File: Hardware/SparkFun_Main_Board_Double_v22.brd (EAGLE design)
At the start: 124.5 x 73.7 mm, 134 parts, among them J1 MICROMOD-2222-C, J10 MICRO-SD-PUSH-PUSH-EXT-PIN, J2 Vertical Qwiic Connector, J4 QWIIC_RIGHT_ANGLE, J5 CORTEX_JTAG_DEBUG_MINIMUM_PTH, J6 MICROMOD_FUNCTION_MAIN, J7 MICROMOD_FUNCTION_MAIN, Q1 3.1A/30V/105mΩ, Q2 20V/4.2A/52mΩ/1.4W, U1 STG3856QTR, U2 MCP73831, U3 ESD Diode, U4 AP7347DQ-33W5-7K-3.3V, U5 AP7361C-33

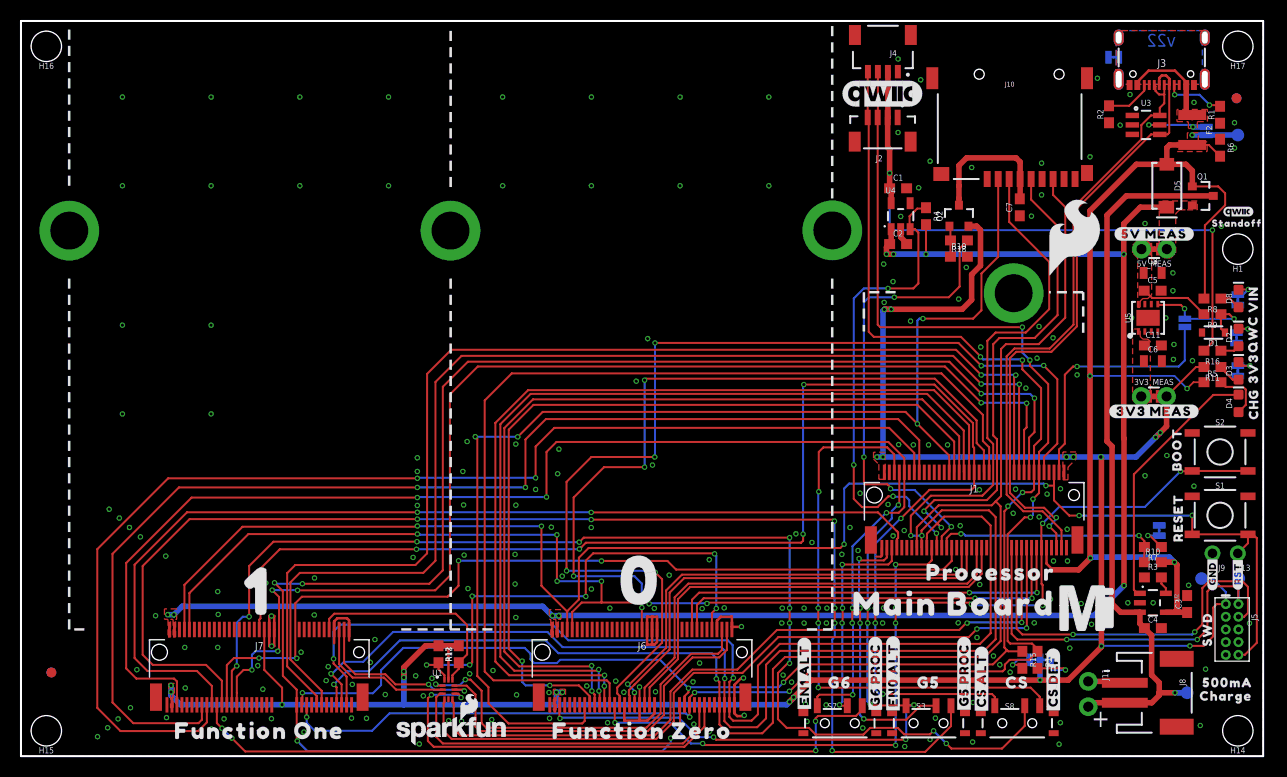
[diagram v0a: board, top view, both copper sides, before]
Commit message: Rotates 2 pin JST connector
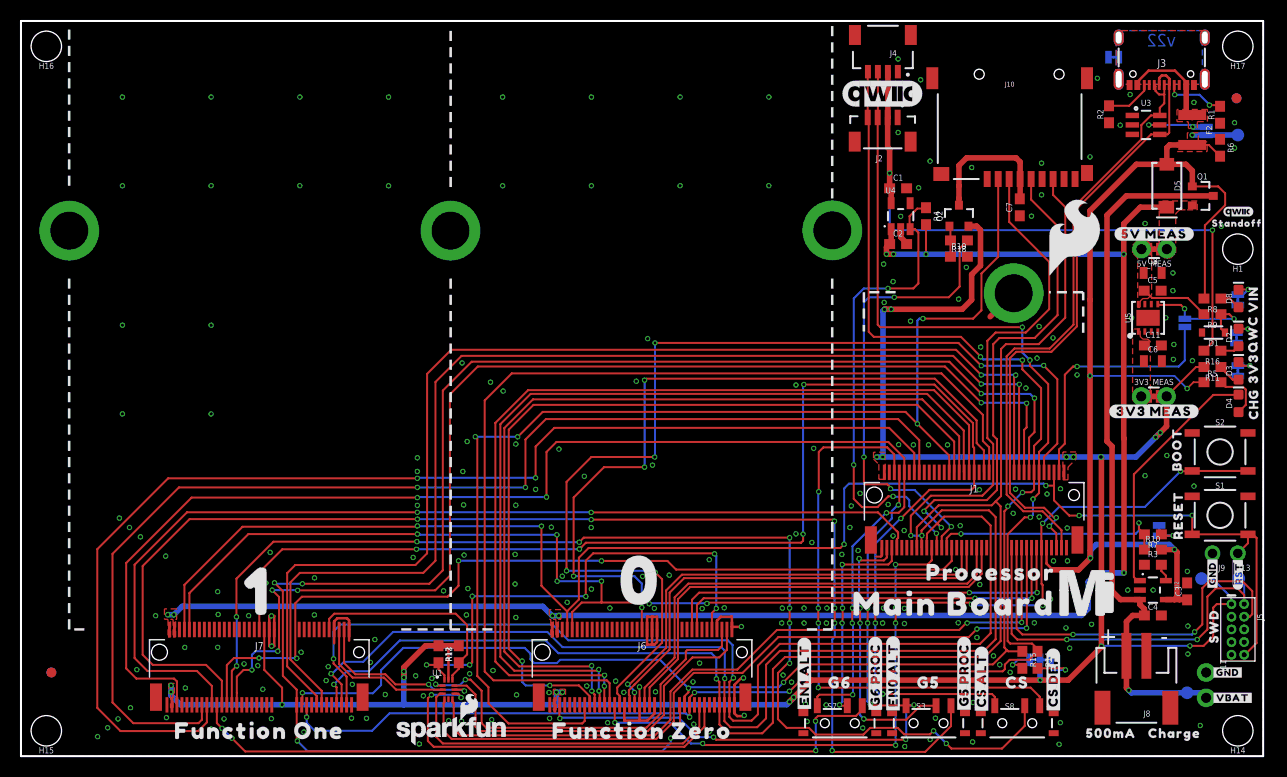
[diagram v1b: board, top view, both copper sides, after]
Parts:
- added U$3: (no value), top:##RST##8
- added U$46: (no value), top:#VBAT#9
- U$39: device top:#RST#6521 -> top:#GND#10
- U$40: device top:#GND#6520 -> top:#GND#10
- moved U$33 12.7 mm to (109.2, 2.29)
- moved J11 11.8 mm to (118.7, 8.38)
- moved U$40 10.0 mm to (120.9, 8.38), turned to 0 degrees
- moved U$27 6.37 mm to (115.6, 2.29)
- moved U$39 2.54 mm to (119.4, 18.3)
- moved J8 2.54 mm to (111.8, 6.35), turned to 180 degrees
- moved U$14 1.52 mm to (106.8, 16.4)
- moved R7 1.27 mm to (113.4, 22.2)
- moved C3 1.27 mm to (116.8, 16.5)
- moved C4 1.27 mm to (113.4, 14.1)
- moved R10 1.27 mm to (113.4, 20.7)
- moved R3 1.27 mm to (113.4, 19.2)
- moved U2 1.27 mm to (113.4, 16.6)
- moved U$25 0.73 mm to (119.5, 13.0)
- moved J5 0.57 mm to (121.9, 12.7)
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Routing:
- net V_BATT: track 73.2 -> 71.3 mm
- net N$14: track 26.1 -> 24.8 mm
- net VCC: track 168.5 -> 169.3 mm
- net VIN/3: track 23.4 -> 24.2 mm
- net 3.3V: track 236.2 -> 237.0 mm
- net VIN: track 112.8 -> 113.6 mm
- net !RESET!: track 155.0 -> 154.4 mm
- net GND: track 49.9 -> 49.6 mm, vias 219 -> 233

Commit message: Pushes JST 0.1" further into the board
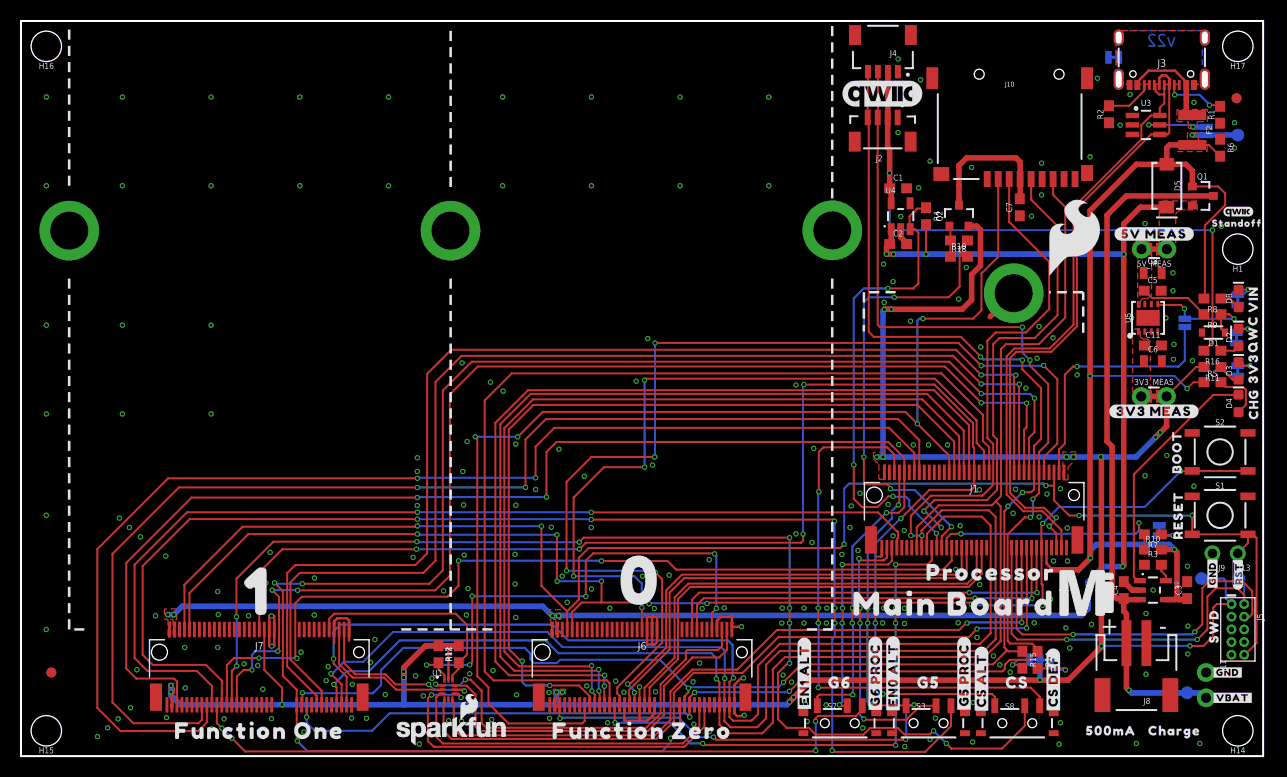
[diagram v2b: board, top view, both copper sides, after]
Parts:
- moved C4 3.87 mm to (110.5, 16.6), turned to 90 degrees
- moved J8 1.27 mm to (111.8, 7.62)
- moved U$8 0.25 mm to (115.8, 30.5)
- moved U$27 0.25 mm to (115.6, 2.54)
- moved U$33 0.25 mm to (109.2, 2.54)
- moved C3 0.13 mm to (116.8, 16.6)
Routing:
- net GND: track 49.6 -> 51.6 mm, vias 233 -> 241
- net V_BATT: track 71.3 -> 70.1 mm
- net 3.3V: track 237.0 -> 237.7 mm

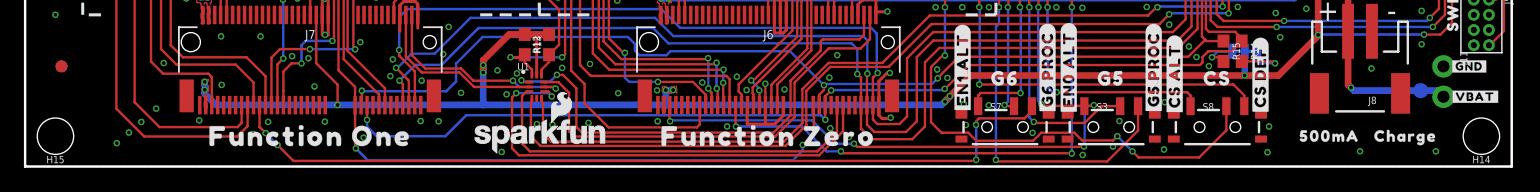
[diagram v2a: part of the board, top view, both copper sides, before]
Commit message: Adds notch for lipo battery, moves VBAT test point
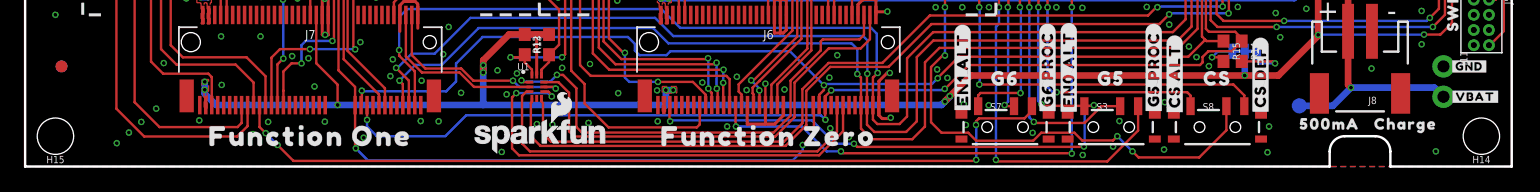
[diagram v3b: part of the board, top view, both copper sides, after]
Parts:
- moved TP3 10.2 mm to (106.7, 5.08)
- moved U$27 1.02 mm to (115.6, 3.56)
- moved U$33 1.02 mm to (109.2, 3.56)
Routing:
- net V_BATT: track 70.1 -> 75.0 mm
- net GND: vias 241 -> 240
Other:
- outline, holes or cut-outs redrawn
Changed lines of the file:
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@@
 <layer number="37" name="tTest" color="7" fill="1" visible="no" active="yes"/>
 <layer number="38" name="bTest" color="7" fill="1" visible="no" active="yes"/>
-<layer number="39" name="tKeepout" color="4" fill="11" visible="yes" active="yes"/>
+<layer number="39" name="tKeepout" color="4" fill="11" visible="no" active="yes"/>
 <layer number="40" name="bKeepout" color="1" fill="11" visible="no" active="yes"/>
 <layer number="41" name="tRestrict" color="4" fill="10" visible="no" active="yes"/>
@@
 <layer number="45" name="Holes" color="7" fill="1" visible="yes" active="yes"/>
 <layer number="46" name="Milling" color="3" fill="1" visible="no" active="yes"/>
-<layer number="47" name="Measures" color="7" fill="1" visible="no" active="yes"/>
+<layer number="47" name="Measures" color="7" fill="1" visible="yes" active="yes"/>
 <layer number="48" name="Document" color="7" fill="1" visible="no" active="yes"/>
 <layer number="49" name="Reference" color="13" fill="1" visible="yes" active="yes"/>
@@
 <plain>
 <wire x1="0" y1="73.66" x2="124.46" y2="73.66" width="0.2032" layer="20"/>
-<wire x1="124.46" y1="0" x2="0" y2="0" width="0.2032" layer="20"/>
+<wire x1="124.46" y1="0" x2="114.3" y2="0" width="0.2032" layer="20"/>
+<wire x1="109.22" y1="0" x2="0" y2="0" width="0.2032" layer="20"/>
 <wire x1="0" y1="0" x2="0" y2="73.66" width="0.2032" layer="20"/>
 <wire x1="124.46" y1="0" x2="124.46" y2="73.66" width="0.2032" layer="20"/>
 <text x="114.2492" y="71.7296" size="1.27" layer="16" font="vector" ratio="15" rot="MR180" align="center">v22</text>
 <text x="63.5" y="-24.384" size="1.778" layer="51" font="vector">Elias Santistevan</text>
-<text x="-0.127" y="-12.319" size="1.778" layer="47" font="vector" ratio="15" rot="R180">Units in Inches</text>
+<text x="-5.207" y="-8.509" size="1.778" layer="47" font="vector" ratio="15" rot="R180">Units in Inches</text>
 <dimension x1="124.46" y1="2.54" x2="0" y2="2.54" x3="62.23" y3="-17.145" textsize="1.778" layer="47" unit="inch"/>
 <dimension x1="0" y1="0" x2="0" y2="73.66" x3="-7.62" y3="36.83" textsize="1.778" layer="47" unit="inch"/>
@@
 <dimension x1="121.92" y1="2.54" x2="124.46" y2="2.54" x3="123.19" y3="-3.81" textsize="1.778" textratio="15" layer="47" dtype="vertical" unit="inch"/>
 <rectangle x1="95.9104" y1="29.4386" x2="96.0374" y2="29.5656" layer="41"/>
+<wire x1="109.22" y1="0" x2="109.22" y2="1.27" width="0.2032" layer="20"/>
+<wire x1="109.22" y1="1.27" x2="110.49" y2="2.54" width="0.2032" layer="20" curve="-90"/>
+<wire x1="110.49" y1="2.54" x2="113.03" y2="2.54" width="0.2032" layer="20"/>
+<wire x1="113.03" y1="2.54" x2="114.3" y2="1.27" width="0.2032" layer="20" curve="-90"/>
+<wire x1="114.3" y1="1.27" x2="114.3" y2="0" width="0.2032" layer="20"/>
+<dimension x1="109.22" y1="1.27" x2="114.3" y2="1.27" x3="111.76" y3="-3.81" textsize="1.778" textratio="15" layer="47" unit="inch"/>
 </plain>
 <attributes>
@@
 </element>
 <element name="TP2" library="SparkFun-Connectors" package="PAD.03X.05" value="TEST-POINT3X5" x="118.287" y="17.792" smashed="yes" rot="MR0"/>
-<element name="TP3" library="SparkFun-Connectors" package="PAD.03X.05" value="TEST-POINT3X5" x="116.84" y="6.35" smashed="yes" rot="MR90"/>
+<element name="TP3" library="SparkFun-Connectors" package="PAD.03X.05" value="TEST-POINT3X5" x="106.68" y="5.08" smashed="yes" rot="MR90"/>
 <element name="TP4" library="SparkFun-Connectors" package="PAD.03X.05" value="TEST-POINT3X5" x="121.92" y="62.23" smashed="yes" rot="MR180"/>
 <element name="TP1" library="SparkFun-Connectors" package="PAD.03X.05" value="TEST-POINT3X5" x="122.016" y="17.802" smashed="yes" rot="MR180"/>
@@
 <element name="U$37" library="top" package="#EN0_ALT#21" value="" x="87.376" y="8.128" smashed="yes" rot="R90"/>
 <element name="U$38" library="top" package="#EN1_ALT#21" value="" x="78.486" y="8.128" smashed="yes" rot="R90"/>
-<element name="U$27" library="top" package="CHARGE501" value="" x="115.57" y="2.54" smashed="yes"/>
+<element name="U$27" library="top" package="CHARGE501" value="" x="115.57" y="3.556" smashed="yes"/>
 <element name="U$7" library="top" package="#SHLD#501" value="" x="112.9792" y="70.0532" smashed="yes" rot="MR0"/>
 <element name="U$30" library="top" package="#I2C#501" value="" x="102.108" y="11.43" smashed="yes" rot="MR0"/>
@@
 <element name="U$26" library="top" package="#3V3_MEAS#6522" value="" x="113.5126" y="34.544" smashed="yes"/>
 <element name="U$31" library="top" package="#5V_MEAS#6522" value="" x="113.538" y="52.324" smashed="yes"/>
-<element name="U$33" library="top" package="500MA6520" value="" x="109.22" y="2.54" smashed="yes"/>
+<element name="U$33" library="top" package="500MA6520" value="" x="109.22" y="3.556" smashed="yes"/>
 <element name="U$19" library="top" package="G518" value="" x="90.932" y="7.366" smashed="yes"/>
 <element name="U$29" library="top" package="G6519" value="" x="82.042" y="7.366" smashed="yes"/>
@@
 <via x="2.54" y="12.7" extent="1-16" drill="0.3048"/>
 <via x="2.54" y="43.18" extent="1-16" drill="0.3048"/>
-<via x="111.76" y="1.27" extent="1-16" drill="0.3048"/>
 <via x="2.54" y="66.04" extent="1-16" drill="0.3048"/>
 <via x="2.54" y="57.15" extent="1-16" drill="0.3048"/>
@@
 <wire x1="110.76" y1="6.842" x2="110.998" y2="6.604" width="0.5588" layer="1"/>
 <via x="110.998" y="6.604" extent="1-16" drill="0.3048"/>
-<wire x1="116.84" y1="6.35" x2="111.252" y2="6.35" width="0.5588" layer="16"/>
-<wire x1="110.998" y1="6.604" x2="111.252" y2="6.35" width="0.5588" layer="16"/>
-<wire x1="116.84" y1="6.35" x2="118.237" y2="6.35" width="0.5588" layer="16"/>
-<wire x1="118.237" y1="6.35" x2="118.745" y2="5.842" width="0.5588" layer="16"/>
 <wire x1="110.76" y1="11.32" x2="110.76" y2="14.247" width="0.5588" layer="1"/>
 <wire x1="110.76" y1="14.247" x2="110.49" y2="14.517" width="0.5588" layer="1"/>
@@
 <wire x1="110.49" y1="15.787" x2="109.7906" y2="15.787" width="0.5588" layer="1"/>
 <wire x1="109.7906" y1="15.787" x2="109.3216" y2="16.256" width="0.5588" layer="1"/>
+<wire x1="106.68" y1="5.08" x2="109.474" y2="5.08" width="0.5588" layer="16"/>
+<wire x1="109.474" y1="5.08" x2="110.998" y2="6.604" width="0.5588" layer="16"/>
+<wire x1="110.998" y1="6.604" x2="117.983" y2="6.604" width="0.5588" layer="16"/>
+<wire x1="117.983" y1="6.604" x2="118.745" y2="5.842" width="0.5588" layer="16"/>
 </signal>
 <signal name="N$14">
